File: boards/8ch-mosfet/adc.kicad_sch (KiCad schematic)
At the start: 9 parts, among them U13 MCP1502, U2 MCP3208, U4 MCP3221A0T

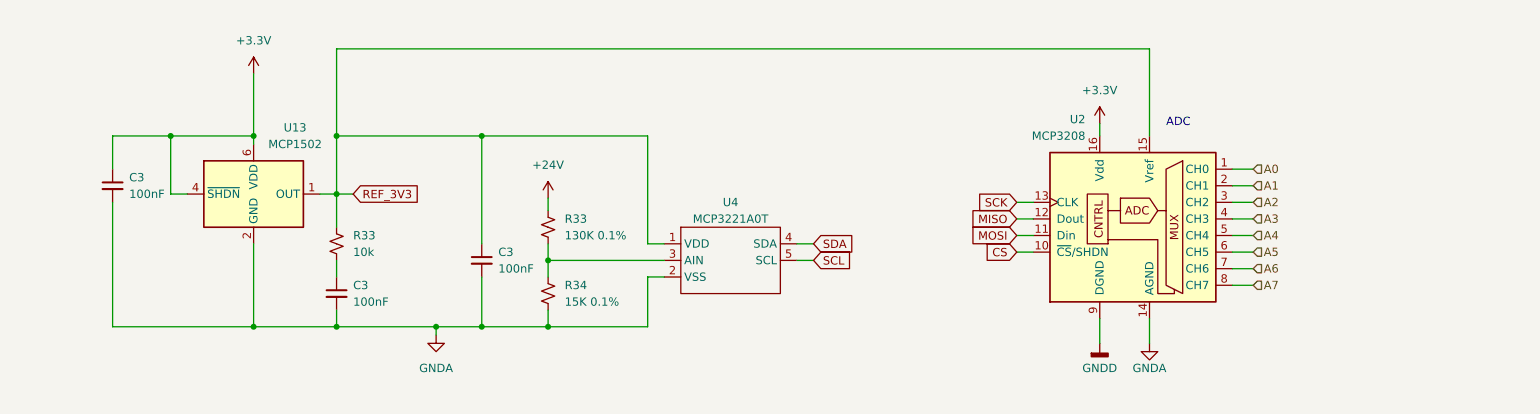
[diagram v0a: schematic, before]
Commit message: tidied up the schematic
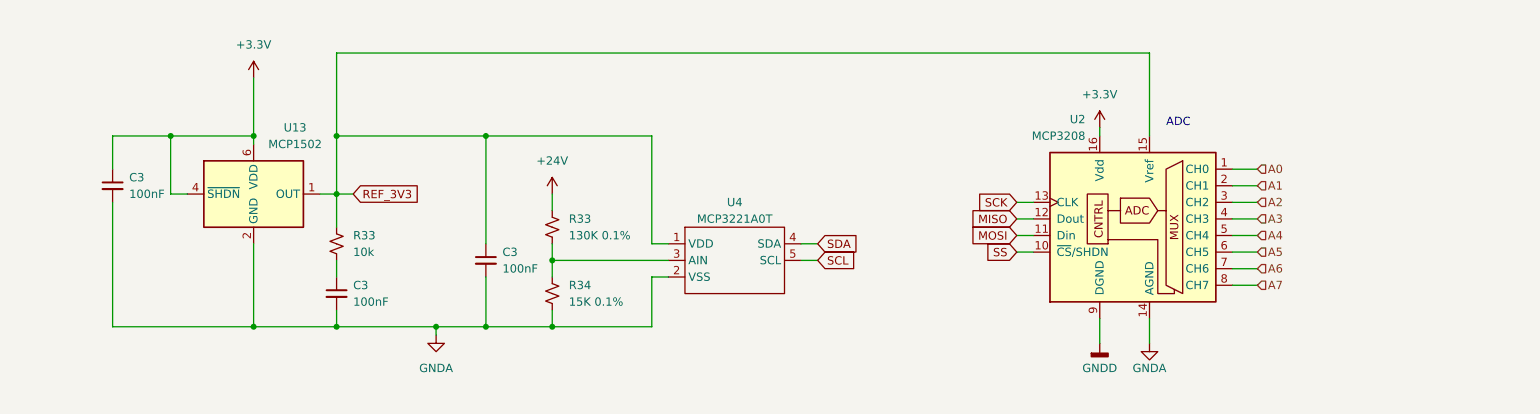
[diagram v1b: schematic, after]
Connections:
- net CS renamed SS
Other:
- moved on the sheet: C3, R33, R34, U4

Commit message: tested the bus voltage stuff a bit more
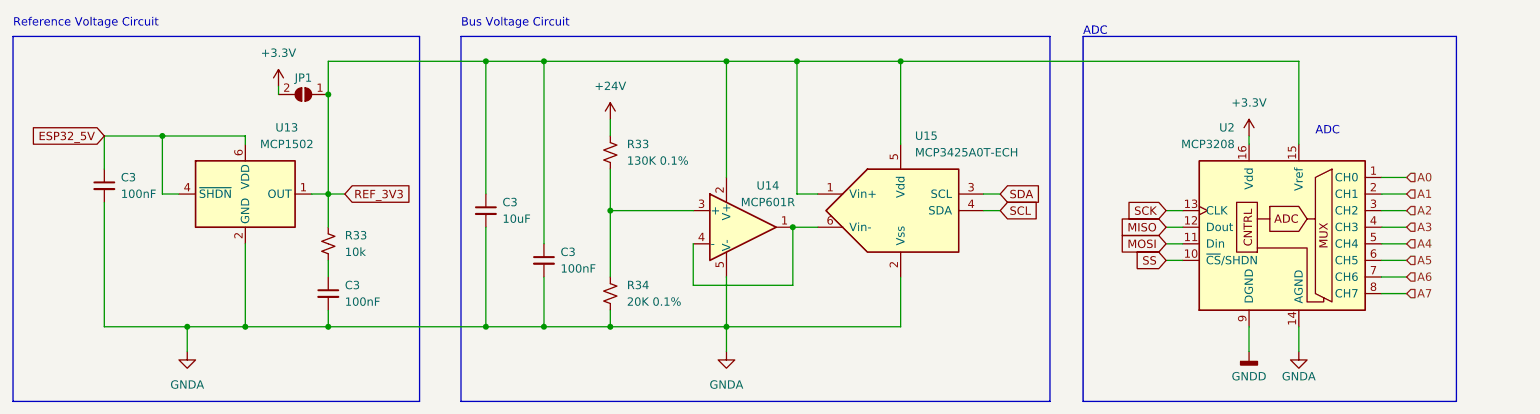
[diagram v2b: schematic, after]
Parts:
- removed U4: MCP3221A0T, Package_TO_SOT_SMD:SOT-23-5, symbol gnarboard:MCP3X21
- added C3: 10uF, Capacitor_SMD:C_0805_2012Metric_Pad1.18x1.45mm_HandSolder, symbol Device:C_Small
- added JP1: SolderJumper_2_Open, Jumper:SolderJumper-2_P1.3mm_Open_RoundedPad1.0x1.5mm, symbol Jumper:SolderJumper_2_Open
- added U14: MCP601R, Package_TO_SOT_SMD:SOT-23-5, symbol Amplifier_Operational:MCP601R
- added U15: MCP3425A0T-ECH, Package_TO_SOT_SMD:SOT-23-6, symbol Analog_ADC:MCP3425A0T-ECH
- R34: value 15K 0.1% -> 20K 0.1%
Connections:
- net +3.3V: now also JP1.2 (B); no longer C3.1, U13.4 (~{SHDN}), U13.6 (VDD)
- net GNDA: now also C3.2, U14.5 (V-), U15.2 (Vss)
- net REF_3V3: now also C3.1, JP1.1 (A), U14.2 (V+), U15.1 (Vin+), U15.5 (Vdd)
- net SCL: now also U15.4 (SDA)
- net SDA: now also U15.3 (SCL)
- net at R33.1, R34.2: now also U14.3 (+)
- new net: U14.1, U14.4 (-), U15.6 (Vin-)
- new net ESP32_5V: C3.1, U13.4 (~{SHDN}), U13.6 (VDD)
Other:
- note added: "Bus Voltage Circuit"
- note added: "Reference Voltage Circuit"
- moved on the sheet: C3, R33, R34, U13, U2

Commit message: some adc changes and then rerouting
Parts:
- removed U14: MCP601R, Package_TO_SOT_SMD:SOT-23-5, symbol Amplifier_Operational:MCP601R
- added C3: 100nF, Capacitor_SMD:C_0805_2012Metric_Pad1.18x1.45mm_HandSolder, symbol Device:C_Small
- added D39: BAT54S, Package_TO_SOT_SMD:SOT-23, symbol Diode:BAT54S
- R33: value 130K 0.1% -> 300K 0.1%
- R34: value 20K 0.1% -> 22K 0.1%
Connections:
- net GNDA: now also U15.6 (Vin-), C3.2, D39.1 (A)
- net REF_3V3: now also C3.1, D39.2 (K); no longer U15.1 (Vin+)
- net at R33.1, R34.2: now also U15.1 (Vin+), D39.3 (COM)
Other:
- moved on the sheet: C3, R34

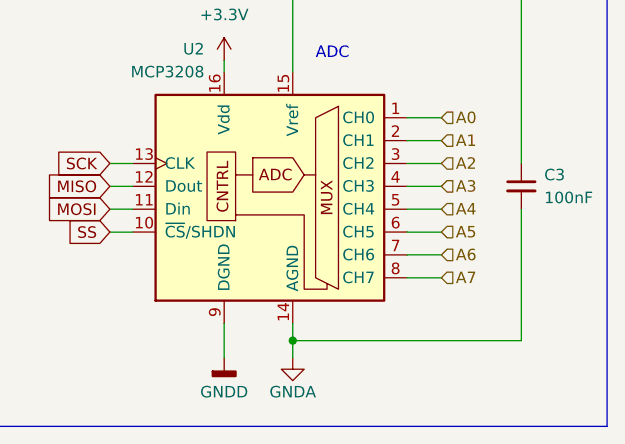
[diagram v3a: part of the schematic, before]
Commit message: added 5v fuse to schematic
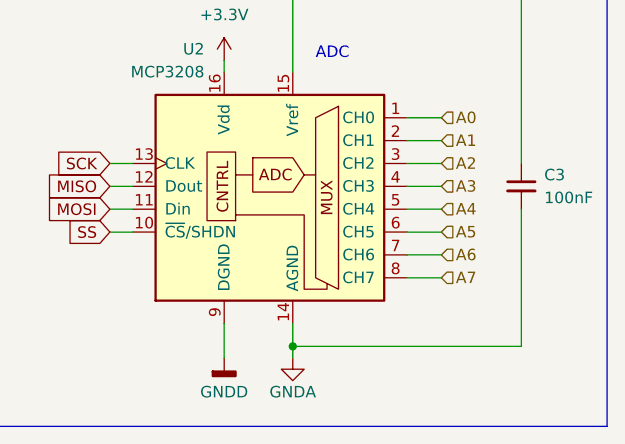
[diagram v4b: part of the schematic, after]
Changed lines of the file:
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@@
   (junction (at 232.41 62.23) (diameter 0) (color 0 0 0 0)
   )
+  (junction (at 232.41 105.41) (diameter 0) (color 0 0 0 0)
+  )
   (junction (at 107.95 62.23) (diameter 0) (color 0 0 0 0)
   )
@@
   (junction (at 139.7 82.55) (diameter 0) (color 0 0 0 0)
   )
-  (junction (at 232.41 104.775) (diameter 0) (color 0 0 0 0)
-  )
   (junction (at 71.12 102.87) (diameter 0) (color 0 0 0 0)
   )
@@
     (stroke (width 0) (type default))
   )
-  (wire (pts (xy 257.81 90.17) (xy 257.81 104.775))
+  (wire (pts (xy 257.81 90.17) (xy 257.81 105.41))
     (stroke (width 0) (type default))
   )
@@
     (stroke (width 0) (type default))
   )
+  (wire (pts (xy 232.41 105.41) (xy 232.41 106.68))
+    (stroke (width 0) (type default))
+  )
   (wire (pts (xy 107.95 62.23) (xy 116.84 62.23))
     (stroke (width 0) (type default))
@@
     (stroke (width 0) (type default))
   )
-  (wire (pts (xy 232.41 104.775) (xy 232.41 106.68))
+  (wire (pts (xy 232.41 102.87) (xy 232.41 105.41))
     (stroke (width 0) (type default))
   )
@@
     (stroke (width 0) (type default))
   )
-  (wire (pts (xy 232.41 102.87) (xy 232.41 104.775))
-    (stroke (width 0) (type default))
-  )
   (wire (pts (xy 245.11 85.09) (xy 248.92 85.09))
     (stroke (width 0) (type default))
   )
-  (wire (pts (xy 257.81 104.775) (xy 232.41 104.775))
-    (stroke (width 0) (type default))
-  )
+  (wire (pts (xy 257.81 105.41) (xy 232.41 105.41))
+    (stroke (width 0) (type default))
+  )

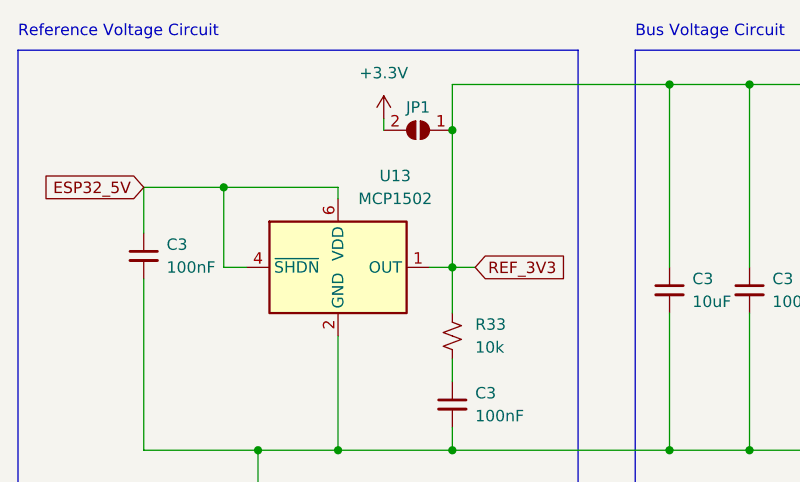
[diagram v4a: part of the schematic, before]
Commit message: prepared 8ch mosfet for production
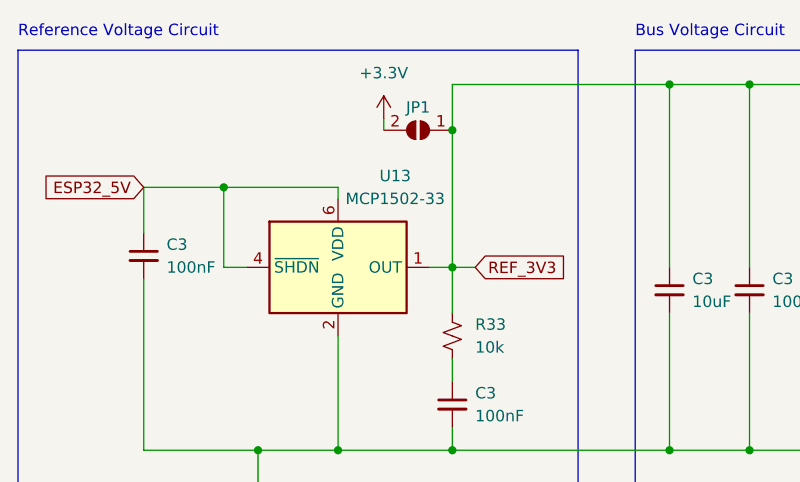
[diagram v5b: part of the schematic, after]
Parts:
- U13: value MCP1502 -> MCP1502-33; Mouser (none) -> 579-MCP1502T-33E/CHY
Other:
- company: (none) -> https://github.com/hoeken/yarrboard
- title: (none) -> Yarrboard 8ch Mosfet Driver
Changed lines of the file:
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@@
 (kicad_sch (version 20230121) (generator eeschema)
   (paper "A4")
+  (title_block
+    (title "Yarrboard 8ch Mosfet Driver")
+    (company "https://github.com/hoeken/yarrboard")
+  )
   (junction (at 107.95 102.87) (diameter 0) (color 0 0 0 0)
   )
@@
       (effects (font (size 1.27 1.27)))
     )
-    (property "Value" "MCP1502" (at 77.47 74.93 0)
+    (property "Value" "MCP1502-33" (at 77.47 74.93 0)
       (effects (font (size 1.27 1.27)))
     )
@@
       (effects (font (size 1.27 1.27)) hide)
     )
+    (property "Mouser" "579-MCP1502T-33E/CHY" (at 71.12 82.55 0)
+      (effects (font (size 1.27 1.27)) hide)
+    )

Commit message: updated BOM
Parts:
- C3: Mouser (none) -> 08053C104KAT4A; Vendor C0805C102J1HACTU -> (none)
- D39: LCSC (none) -> C727126
- JP1: now left out of the parts list
- R33: LCSC (none) -> C865386
- R33: Vendor 652-CR0805JW-104ELF -> (none)
- R34: LCSC (none) -> C865312
- U15: Mouser (none) -> 579-MCP3425A0T-E/CH
- U2: Mouser (none) -> MCP3208T-BI/SL; Vendor MCP3208T-BI/SL -> (none)
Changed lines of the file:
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@@
       (effects (font (size 1.27 1.27)) hide)
     )
-    (property "Vendor" "MCP3208T-BI/SL" (at 229.87 87.63 0)
+    (property "Mouser" "MCP3208T-BI/SL" (at 229.87 87.63 0)
       (effects (font (size 1.27 1.27)) hide)
     )
@@
       (effects (font (size 1.27 1.27)) hide)
     )
-    (property "Vendor" "" (at 127 76.2 0)
+    (property "LCSC" "C865386" (at 127 76.2 0)
       (effects (font (size 1.27 1.27)) hide)
     )
@@
     )
     (property "Datasheet" "~" (at 83.82 90.17 0)
-      (effects (font (size 1.27 1.27)) hide)
-    )
-    (property "Vendor" "652-CR0805JW-104ELF" (at 83.82 90.17 0)
       (effects (font (size 1.27 1.27)) hide)
     )
@@
       (effects (font (size 1.27 1.27)) hide)
     )
-    (property "Vendor" "C0805C102J1HACTU" (at 257.81 87.63 0)
+    (property "Mouser" "08053C104KAT4A" (at 257.81 87.63 0)
       (effects (font (size 1.27 1.27)) hide)
     )
@@
       (effects (font (size 1.27 1.27)) hide)
     )
-    (property "Vendor" "C0805C102J1HACTU" (at 83.82 97.79 0)
+    (property "Mouser" "08053C104KAT4A" (at 83.82 97.79 0)
       (effects (font (size 1.27 1.27)) hide)
     )
@@
   )
   (symbol (lib_id "Jumper:SolderJumper_2_Open") (at 80.01 67.31 180) (unit 1)
-    (in_bom yes) (on_board yes) (dnp no)
+    (in_bom no) (on_board yes) (dnp no)
     (property "Reference" "JP1" (at 80.01 64.77 0)
       (effects (font (size 1.27 1.27)))
@@
     )
     (property "Datasheet" "http://ww1.microchip.com/downloads/en/DeviceDoc/22072b.pdf" (at 171.45 85.09 0)
+      (effects (font (size 1.27 1.27)) hide)
+    )
+    (property "Mouser" " 579-MCP3425A0T-E/CH " (at 171.45 85.09 0)
       (effects (font (size 1.27 1.27)) hide)
     )
@@
       (effects (font (size 1.27 1.27)) hide)
     )
-    (property "Vendor" "C0805C102J1HACTU" (at 116.84 85.09 0)
+    (property "Mouser" "08053C104KAT4A" (at 116.84 85.09 0)
       (effects (font (size 1.27 1.27)) hide)
     )
@@
       (effects (font (size 1.27 1.27)) hide)
     )
-    (property "Vendor" "" (at 127 88.9 0)
+    (property "LCSC" "C865312" (at 127 88.9 0)
       (effects (font (size 1.27 1.27)) hide)
     )
@@
       (effects (font (size 1.27 1.27)) hide)
     )
+    (property "LCSC" "C727126" (at 144.78 82.55 90)
+      (effects (font (size 1.27 1.27)) hide)
+    )
     (pin "1")
     (pin "2")
@@
       (effects (font (size 1.27 1.27)) hide)
     )
-    (property "Vendor" "C0805C102J1HACTU" (at 49.53 81.28 0)
-      (effects (font (size 1.27 1.27)) hide)
-    )
+    (property "Mouser" "08053C104KAT4A" (at 49.53 81.28 0)
+      (effects (font (size 1.27 1.27)) hide)
+    )

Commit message: more BOM updates.
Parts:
- C3: LCSC (none) -> C49678
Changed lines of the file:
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@@
+      (effects (font (size 1.27 1.27)) hide)
+    )
+    (property "LCSC" "C49678" (at 83.82 97.79 0)
       (effects (font (size 1.27 1.27)) hide)
     )
@@
       (effects (font (size 1.27 1.27)) hide)
     )
+    (property "LCSC" "C49678" (at 116.84 85.09 0)
+      (effects (font (size 1.27 1.27)) hide)
+    )
     (pin "1")
     (pin "2")
@@
       (effects (font (size 1.27 1.27)) hide)
     )
+    (property "LCSC" "C49678" (at 49.53 81.28 0)
+      (effects (font (size 1.27 1.27)) hide)
+    )

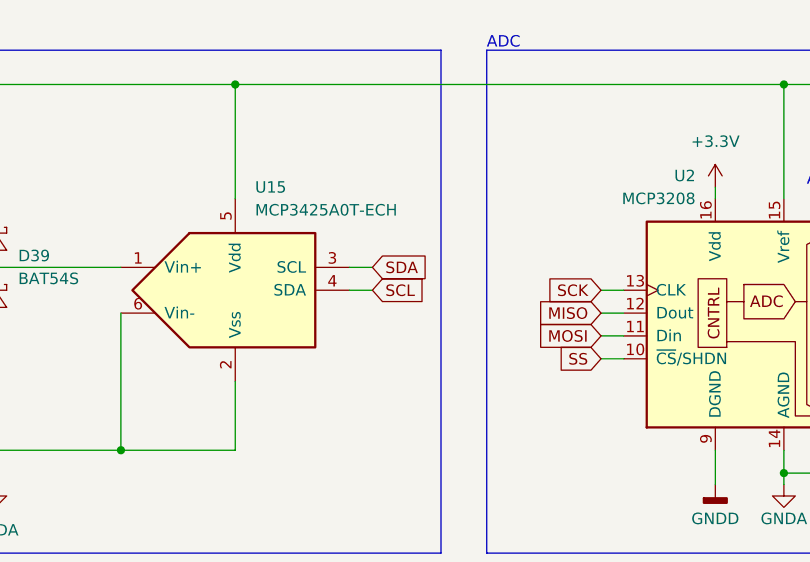
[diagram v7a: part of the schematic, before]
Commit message: damnit, messed up the sda/scl lines on the board
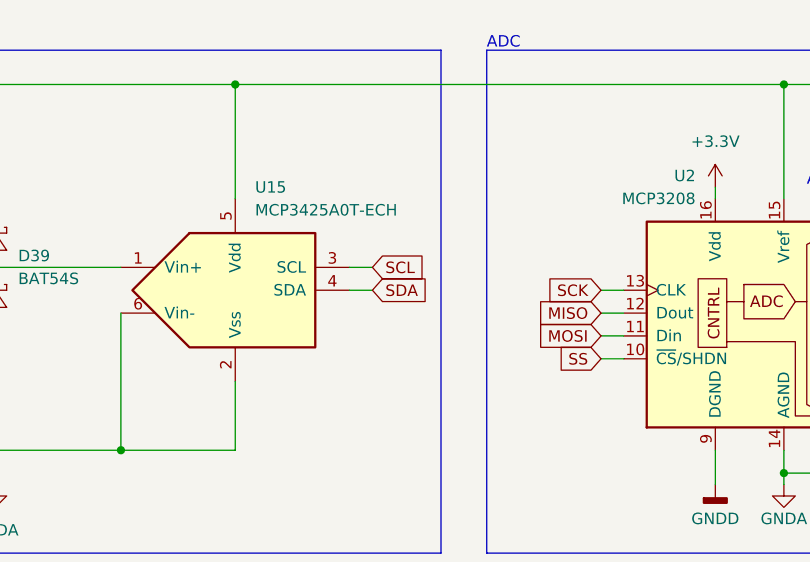
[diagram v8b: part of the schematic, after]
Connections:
- net SCL: now also U15.3 (SCL); no longer U15.4 (SDA)
- net SDA: now also U15.4 (SDA); no longer U15.3 (SCL)
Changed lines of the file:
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@@
     )
   )
-  (global_label "SDA" (shape input) (at 186.69 82.55 0) (fields_autoplaced)
+  (global_label "SCL" (shape input) (at 186.69 82.55 0) (fields_autoplaced)
     (effects (font (size 1.27 1.27)) (justify left))
-    (property "Intersheetrefs" "${INTERSHEET_REFS}" (at 193.2433 82.55 0)
+    (property "Intersheetrefs" "${INTERSHEET_REFS}" (at 193.1828 82.55 0)
       (effects (font (size 1.27 1.27)) (justify left) hide)
     )
@@
     )
   )
-  (global_label "SCL" (shape input) (at 186.69 85.09 0) (fields_autoplaced)
+  (global_label "SDA" (shape input) (at 186.69 85.09 0) (fields_autoplaced)
     (effects (font (size 1.27 1.27)) (justify left))
-    (property "Intersheetrefs" "${INTERSHEET_REFS}" (at 193.1828 85.09 0)
+    (property "Intersheetrefs" "${INTERSHEET_REFS}" (at 193.2433 85.09 0)
       (effects (font (size 1.27 1.27)) (justify left) hide)
     )
